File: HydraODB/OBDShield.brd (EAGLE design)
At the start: 59.9 x 37 mm, 9 parts, among them J1 HYDRABUS_SHIELD_CON_HEADER_2X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, J2 HYDRABUS_SHIELD_CON_HEADER_2X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, J3 HYDRABUS_SHIELD_CON_HEADER_2X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, U1 SN65HVD233D, U2 SN65HVD233D

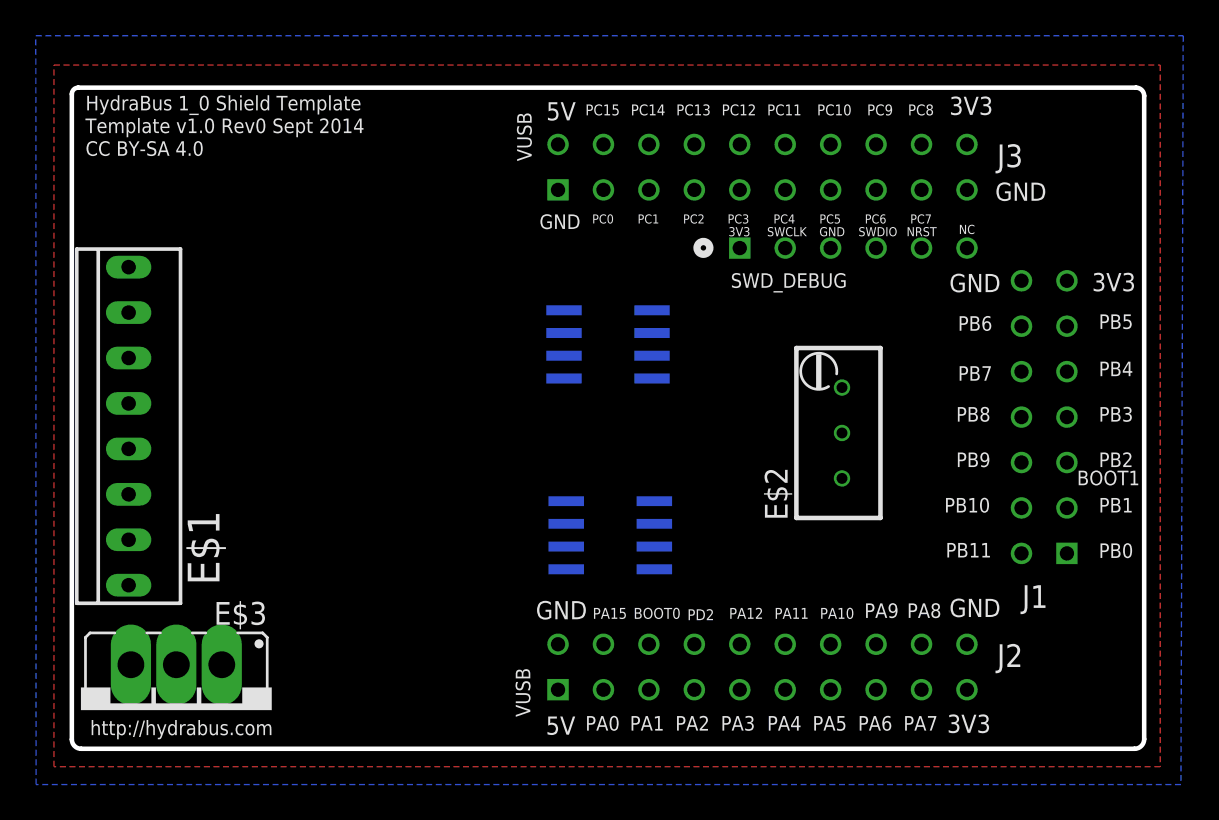
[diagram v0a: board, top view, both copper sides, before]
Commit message: Rebuilt everything, schema and board were inconsistent. First try at PCB routing.
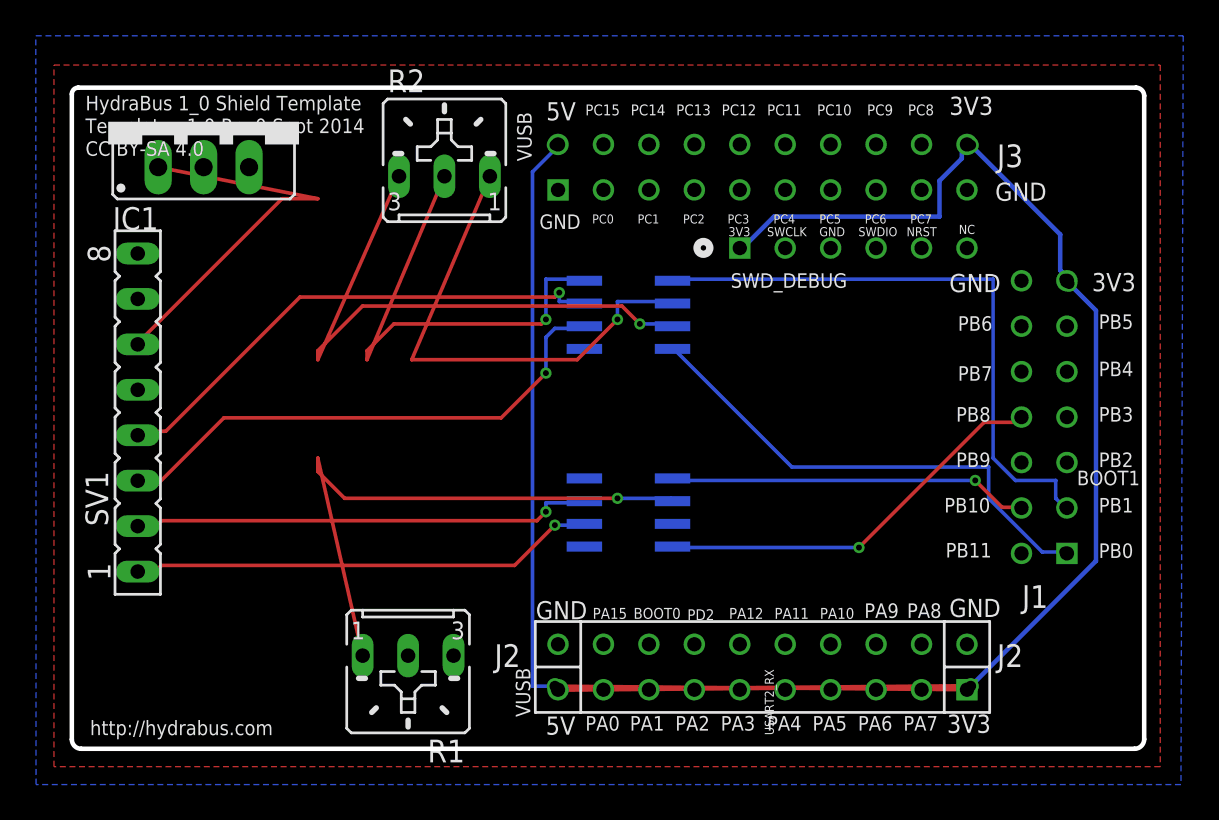
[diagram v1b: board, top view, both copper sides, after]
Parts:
- removed E$1: (no value), con-conrad:741256-49
- removed E$2: (no value), ref-packages:RTRIMT93YA
- removed E$3: (no value), v-reg:79XXS_
- added IC1: (no value), v-reg:78XXS
- added R1, R2: (no value), pot:B25U
- added SV1: (no value), con-lsta:FE08
- U1, U2: value SN65HVD233D -> SN65HVD233DG4
- moved U2 12.4 mm to (31.1, 24.3)
- moved U1 9.47 mm to (31.1, 13.2)
- flipped J2 to the bottom
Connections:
- removed net PB1: J1.3
- new net +12V: IC1.IN, SV1.6
- new net N$10: SV1.2, U1.7
- new net N$11: SV1.3, U2.6
- new net N$12: SV1.4, U2.7
- new net N$13: IC1.GND
- new net N$14: R2.A, U2.2
- new net N$16: R1.S
- new net N$17: R2.S, U2.8
- new net N$18: U2.5
- new net N$20: J1.3, U2.1
- new net N$4: IC1.OUT
- new net N$6: R2.E, U2.3
- new net N$7: R1.A, U1.2
- new net N$9: SV1.1, U1.6
- net +3V3: no longer U2.3
- net GND: now also SV1.5, U1.5; no longer U1.2, U1.8, U2.2, U2.8
- net PB0: now also U2.4
- net PB10: now also U1.1
- net PB8: now also U1.4
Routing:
- net +3V3: track 0.00 -> 76.0 mm, vias 0 -> 5
- net VUSB: track 0.00 -> 55.2 mm, vias 0 -> 2
- net N$20: track 0.00 -> 33.8 mm, vias 0 -> 1
- net N$6: track 0.00 -> 33.1 mm, vias 0 -> 1
- net N$7: track 0.00 -> 32.6 mm, vias 0 -> 1
- net N$11: track 0.00 -> 30.0 mm, vias 0 -> 1
- net N$12: track 0.00 -> 28.9 mm, vias 0 -> 1
- net PB0: track 0.00 -> 27.8 mm, vias 0 -> 1
- net N$14: track 0.00 -> 27.7 mm, vias 0 -> 1
- net N$17: track 0.00 -> 26.8 mm, vias 0 -> 1
- net N$9: track 0.00 -> 26.1 mm, vias 0 -> 1
- net N$10: track 0.00 -> 25.8 mm, vias 0 -> 1
- net +12V: track 0.00 -> 22.6 mm
- net PB8: track 0.00 -> 22.5 mm, vias 0 -> 2
- net PB10: track 0.00 -> 20.2 mm, vias 0 -> 2

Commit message: board pcb routing tryout
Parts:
- moved R2 12.6 mm to (16.1, 21.2)
- moved R1 10.3 mm to (16.1, 14.2)
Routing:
- net N$7: track 32.6 -> 22.4 mm
- net N$6: track 33.1 -> 23.3 mm
- net N$14: track 27.7 -> 18.0 mm
- net N$17: track 26.8 -> 17.1 mm
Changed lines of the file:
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@@
 <?xml version="1.0" encoding="utf-8"?>
 <!DOCTYPE eagle SYSTEM "eagle.dtd">
-<eagle version="7.3.0">
+<eagle version="7.4.0">
 <drawing>
 <settings>
@@
 </element>
 <element name="IC1" library="v-reg" package="78XXS" value="" x="7.366" y="35.052"/>
-<element name="R1" library="pot" package="B25U" value="" x="18.796" y="4.318" rot="R180"/>
-<element name="R2" library="pot" package="B25U" value="" x="20.828" y="32.893"/>
+<element name="R1" library="pot" package="B25U" value="" x="16.129" y="14.224" rot="R180"/>
+<element name="R2" library="pot" package="B25U" value="" x="16.129" y="21.209"/>
 <element name="SV1" library="con-lsta" package="FE08" value="" x="3.683" y="18.796" rot="R90">
 <attribute name="MPN" value="" x="3.683" y="18.796" size="1.778" layer="27" rot="R90" display="off"/>
@@
 <wire x1="13.75" y1="21.75" x2="13.75" y2="22.25" width="0.2032" layer="1"/>
 <wire x1="33.5" y1="23.75" x2="33.5788" y2="23.622" width="0.2032" layer="16"/>
-<wire x1="13.75" y1="21.75" x2="18.288" y2="32.004" width="0.2032" layer="1"/>
+<wire x1="13.75" y1="21.75" x2="13.589" y2="20.32" width="0.2032" layer="1"/>
 <via x="31.75" y="23.75" extent="1-16" drill="0.3302"/>
 </signal>
@@
 <wire x1="13.75" y1="16.25" x2="13.75" y2="15.5" width="0.2032" layer="1"/>
 <wire x1="33.5" y1="14" x2="33.5788" y2="13.843" width="0.2032" layer="16"/>
-<wire x1="13.75" y1="16.25" x2="16.256" y2="5.207" width="0.2032" layer="1"/>
+<wire x1="13.75" y1="16.25" x2="13.589" y2="15.113" width="0.2032" layer="1"/>
 <via x="30.5" y="14" extent="1-16" drill="0.3302"/>
 </signal>
@@
 <wire x1="19" y1="21.75" x2="28.25" y2="21.75" width="0.2032" layer="1"/>
 <wire x1="33.5" y1="25" x2="33.5788" y2="24.892" width="0.2032" layer="16"/>
-<wire x1="19" y1="21.75" x2="23.368" y2="32.004" width="0.2032" layer="1"/>
+<wire x1="19" y1="21.75" x2="18.669" y2="20.32" width="0.2032" layer="1"/>
 <via x="30.5" y="24" extent="1-16" drill="0.3302"/>
 </signal>
@@
 <wire x1="16.5" y1="21.75" x2="16.5" y2="22.25" width="0.2032" layer="1"/>
 <wire x1="28.5" y1="26.25" x2="28.6512" y2="26.162" width="0.2032" layer="16"/>
-<wire x1="16.5" y1="21.75" x2="20.828" y2="32.004" width="0.2032" layer="1"/>
+<wire x1="16.5" y1="21.75" x2="16.129" y2="20.32" width="0.2032" layer="1"/>
 <via x="26.5" y="24" extent="1-16" drill="0.3302"/>
 </signal>

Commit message: Placing and routing
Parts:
- moved R2 6.13 mm to (17.5, 27.2)
- moved R1 5.35 mm to (16.5, 8.89)
- moved SV1 2.50 mm to (4.70, 16.5)
- moved IC1 2.42 mm to (7.49, 32.6)
- moved U2 1.31 mm to (30.5, 23.1)
- moved U1 0.81 mm to (30.5, 13.7), turned to 180 degrees
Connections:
- removed net N$13: IC1.GND
- removed net N$14: R2.A, U2.2
- removed net N$16: R1.S
- removed net N$18: U2.5
- removed net N$20: J1.3, U2.1
- removed net N$4: IC1.OUT
- removed net N$6: R2.E, U2.3
- removed net N$7: R1.A, U1.2
- removed net PB0: J1.1, U2.4
- net +3V3: now also R1.E, R2.E, U1.3, U2.3
- net GND: now also IC1.GND, R1.A, R2.A, U1.2, U2.2, U2.5
- net N$1: now also R1.S, U1.8; no longer U1.3
- net PB10: now also J1.6; no longer J1.4
- net PB11: now also J1.4, U2.1; no longer J1.2
- net PB9: now also J1.2, U2.4; no longer J1.6
- net VUSB: now also IC1.OUT
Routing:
- net N$20: track 33.8 -> 0.00 mm, vias 1 -> 0
- net PB11: track 0.00 -> 29.8 mm
- net PB0: track 27.8 -> 0.00 mm, vias 1 -> 0
- net N$1: track 0.00 -> 27.1 mm
- net VUSB: track 55.2 -> 80.8 mm, vias 2 -> 0
- net PB9: track 0.00 -> 24.4 mm
- net N$6: track 23.3 -> 0.00 mm, vias 1 -> 0
- net N$7: track 22.4 -> 0.00 mm, vias 1 -> 0
- net PB10: track 20.2 -> 42.2 mm, vias 2 -> 0
- net N$9: track 26.1 -> 46.5 mm, vias 1 -> 0
- net N$10: track 25.8 -> 44.3 mm, vias 1 -> 0
- net N$14: track 18.0 -> 0.00 mm, vias 1 -> 0
- net +3V3: track 76.0 -> 87.9 mm, vias 5 -> 0
- net +12V: track 22.6 -> 11.5 mm
- net PB8: track 22.5 -> 30.4 mm, vias 2 -> 0
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
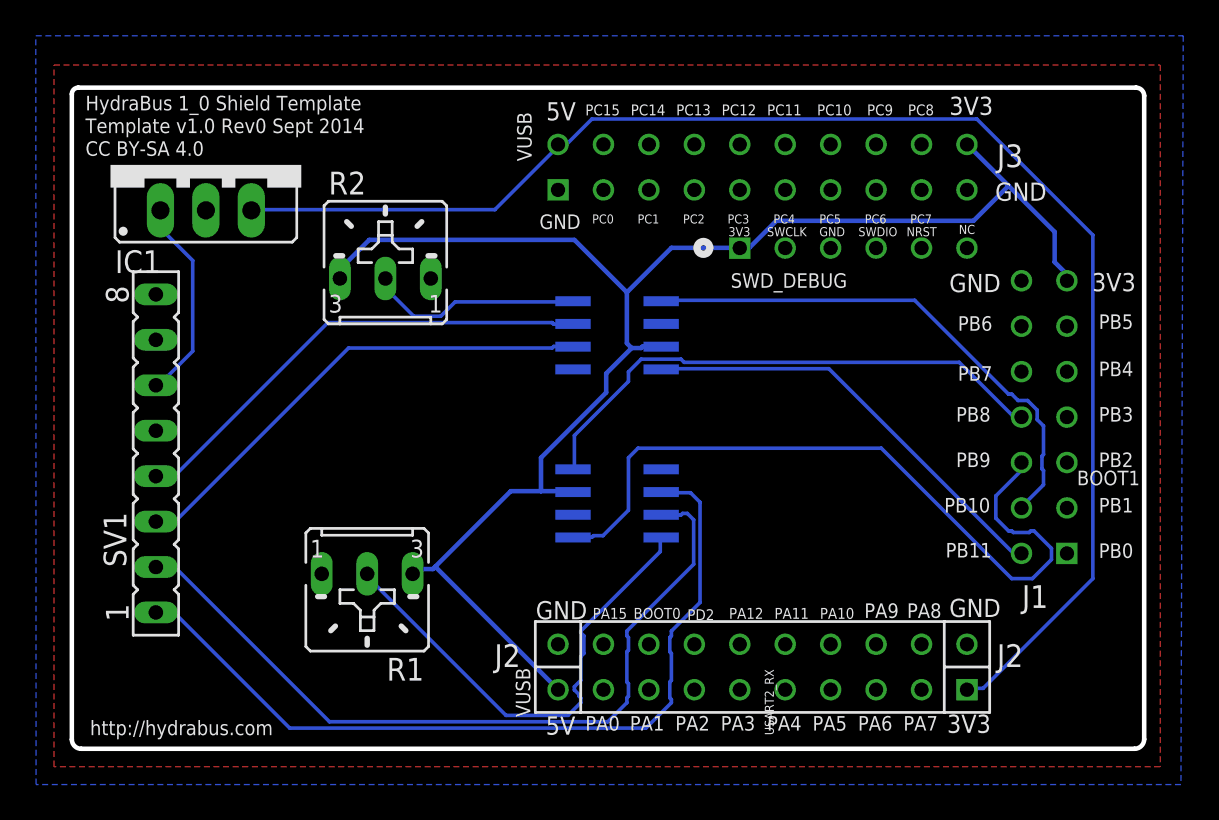
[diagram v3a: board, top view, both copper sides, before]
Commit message: Proto pcb routing
Routing signle layer for proto pcb
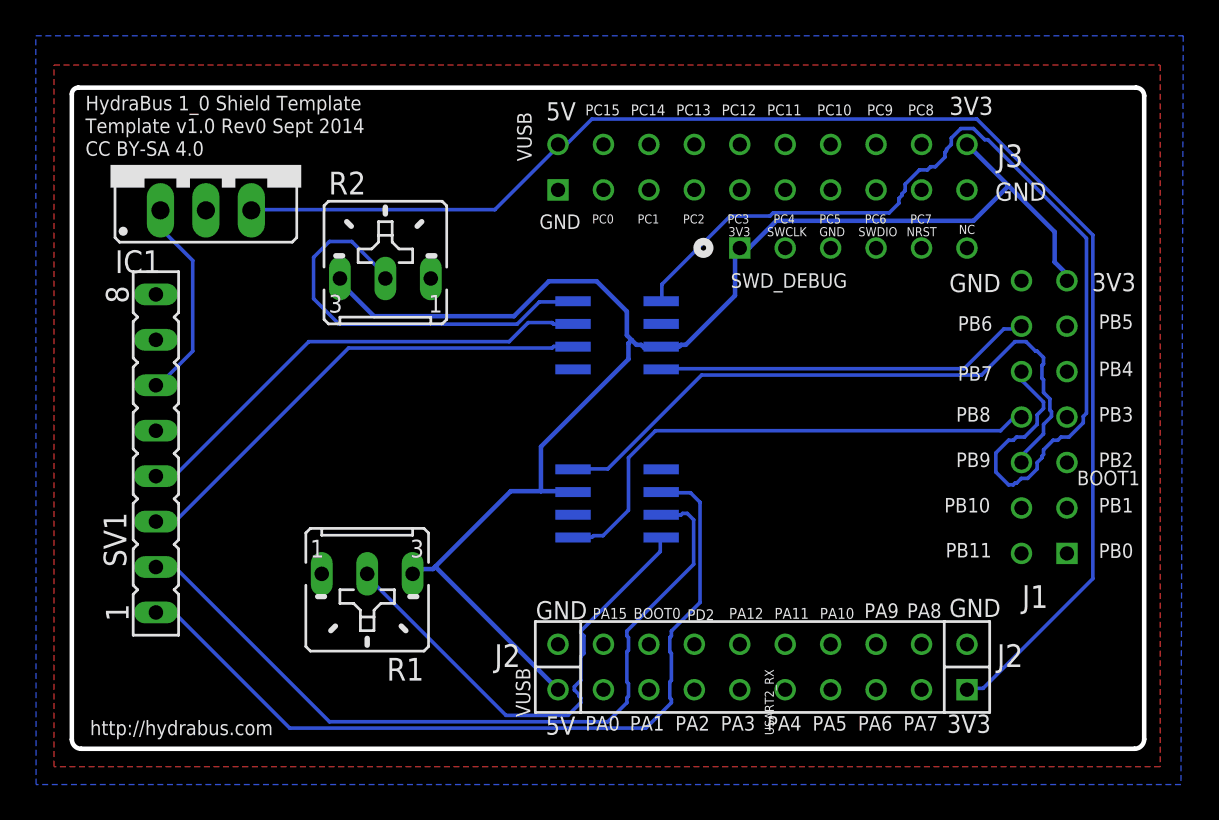
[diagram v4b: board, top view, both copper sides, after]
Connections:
- removed net PB11: J1.4, U2.1
- removed net PB9: J1.2, U2.4
- net PB10: now also J1.8; no longer J1.6
- net PB6: now also U2.4
- net PB7: now also U2.1
- net PB8: now also J1.6; no longer J1.8
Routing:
- net PB7: track 0.00 -> 56.8 mm
- net PB11: track 29.8 -> 0.00 mm
- net PB9: track 24.4 -> 0.00 mm
- net PB6: track 0.00 -> 21.2 mm
- net PB10: track 42.2 -> 29.6 mm
- net N$17: track 12.0 -> 23.3 mm
- net PB8: track 30.4 -> 36.5 mm

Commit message: Schema correction
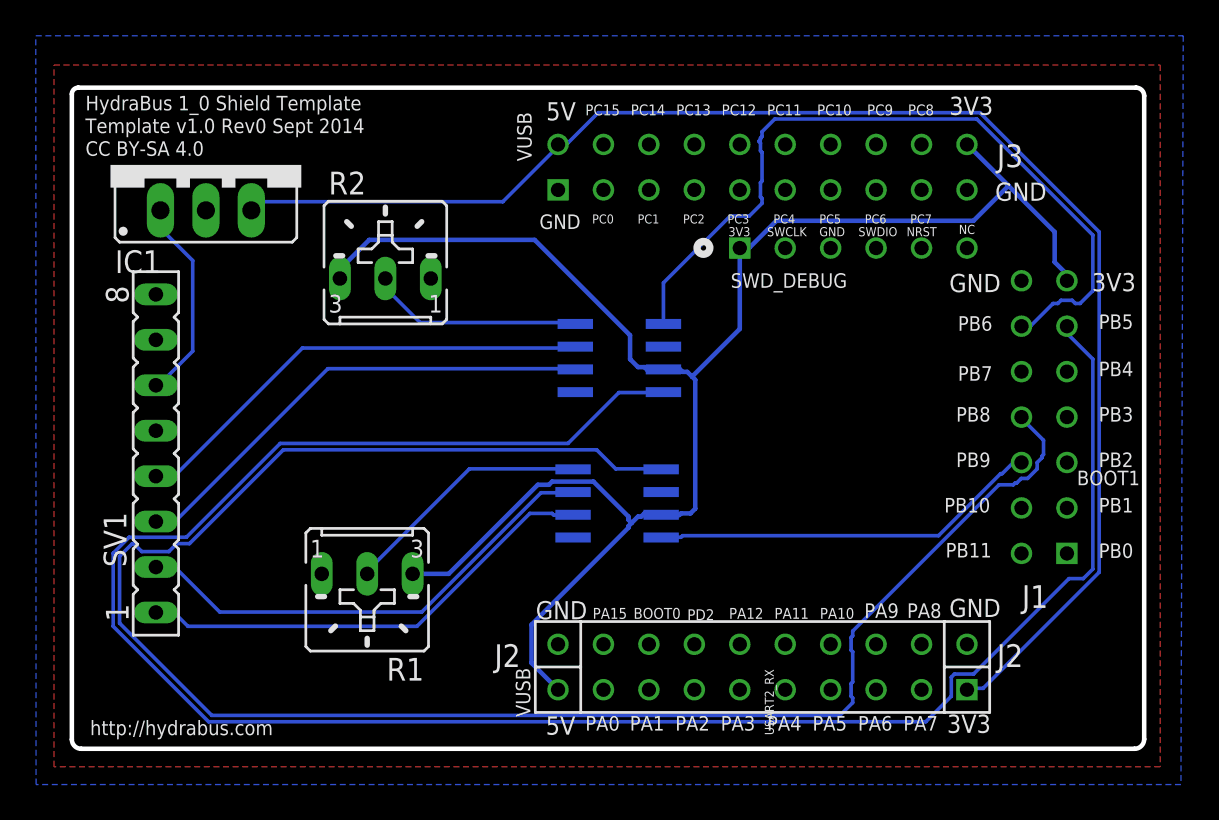
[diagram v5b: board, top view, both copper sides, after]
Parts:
- moved U2 1.28 mm to (30.6, 21.8)
- turned U1 to 0 degrees
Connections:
- removed net PB6: J1.12, U2.4
- net PB5: now also U2.4
- net PB7: now also J1.12; no longer J1.10
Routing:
- net PB5: track 0.00 -> 113.9 mm
- net PB10: track 29.6 -> 102.5 mm
- net PB6: track 21.2 -> 0.00 mm
- net N$9: track 46.5 -> 26.3 mm
- net N$10: track 44.3 -> 27.2 mm
- net PB8: track 36.5 -> 21.9 mm
- net PB7: track 56.8 -> 43.4 mm
- net N$1: track 27.1 -> 14.1 mm
- net N$17: track 23.3 -> 12.0 mm
- net +3V3: track 87.8 -> 98.7 mm
- net VUSB: track 80.8 -> 81.7 mm

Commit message: Corrected J2 mirror
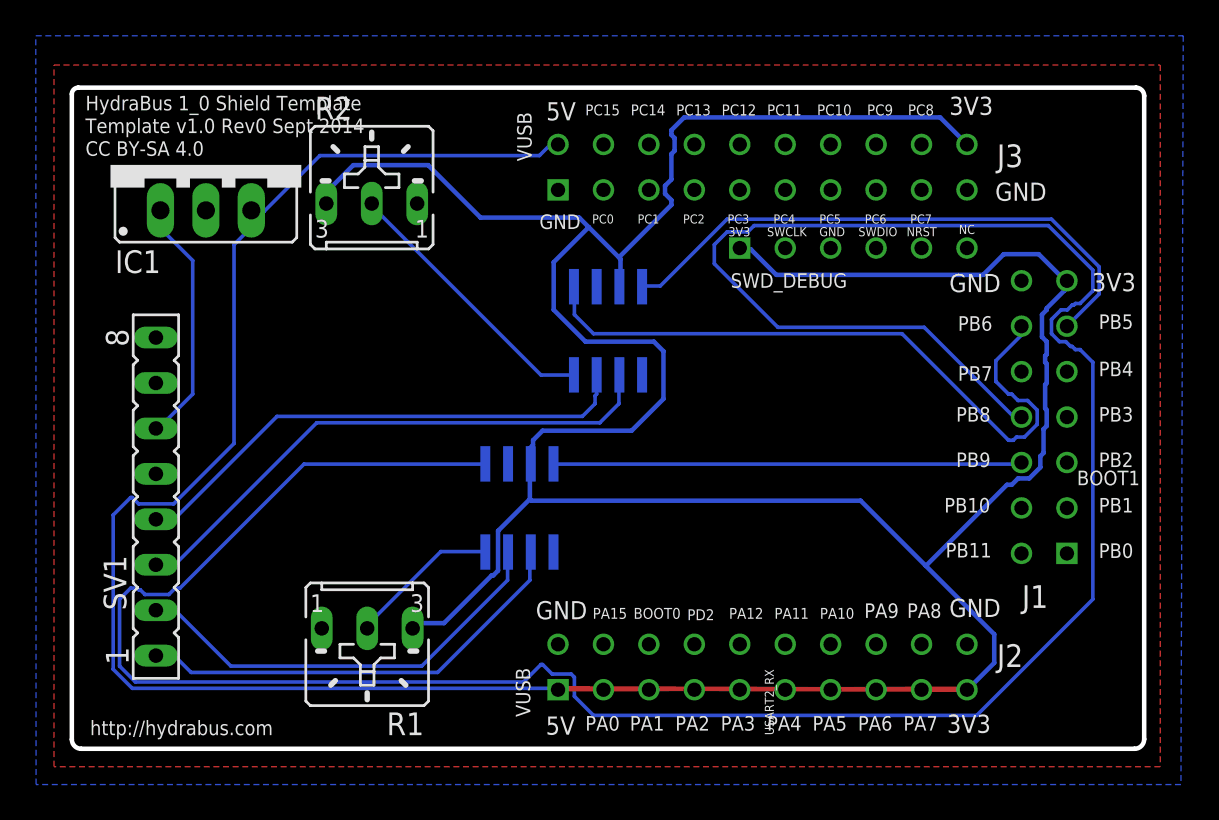
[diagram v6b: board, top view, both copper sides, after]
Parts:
- moved U1 5.47 mm to (25.0, 13.5), turned to 270 degrees
- moved R2 4.26 mm to (16.8, 31.4)
- moved R1 3.05 mm to (16.5, 5.84)
- moved SV1 2.41 mm to (4.70, 14.1)
- moved U2 1.65 mm to (30.0, 23.4), turned to 270 degrees
- flipped J2 to the top
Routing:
- net +3V3: track 98.7 -> 181.4 mm
- net PB5: track 113.9 -> 32.3 mm
- net PB10: track 102.5 -> 152.9 mm
- net VUSB: track 81.7 -> 97.7 mm
- net N$1: track 14.1 -> 8.51 mm
- net PB7: track 43.4 -> 38.2 mm
- net PB8: track 21.9 -> 26.2 mm
- net N$11: track 27.0 -> 31.2 mm
- net N$17: track 12.0 -> 15.4 mm
- net N$10: track 27.2 -> 24.5 mm
- net N$12: track 26.5 -> 28.9 mm
- net +12V: track 11.5 -> 13.9 mm
- net N$9: track 26.3 -> 25.0 mm
